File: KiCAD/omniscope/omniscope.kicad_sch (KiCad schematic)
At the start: 8 parts, among them J1 Conn_01x08_Male, J2 Conn_01x02_Male, J3 Conn_01x02_Male, J4 Conn_01x08_Male, J5 Conn_01x08_Male, J6 Conn_01x08_Male, J7 Conn_01x08_Male, J8 Conn_01x08_Male

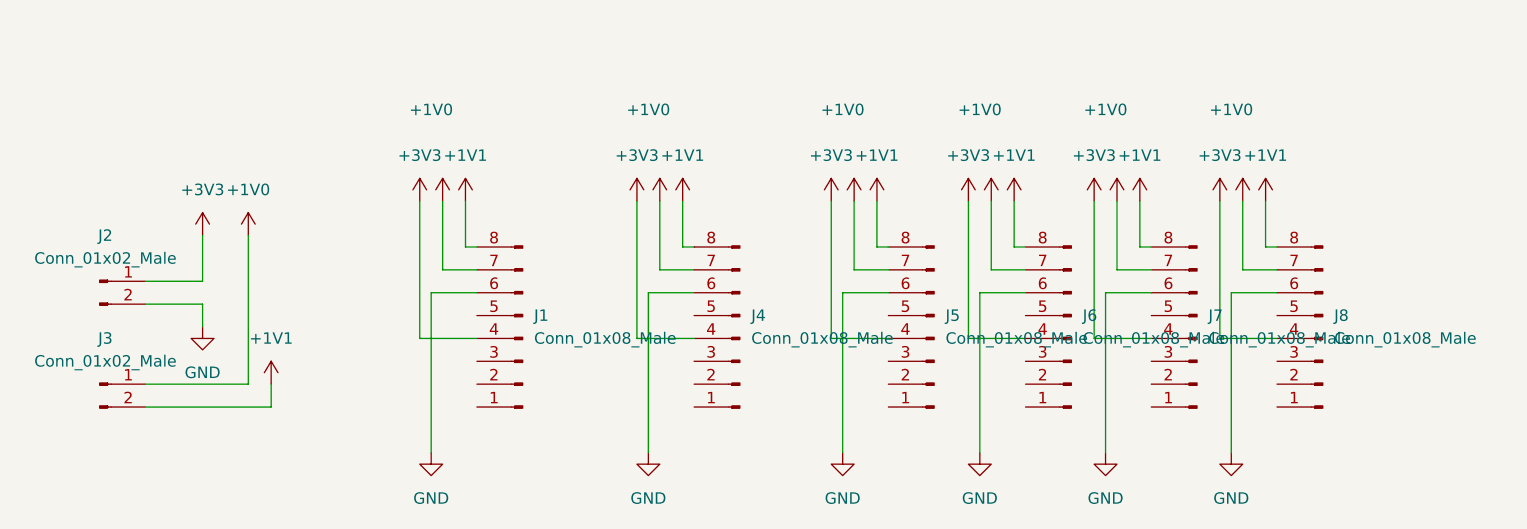
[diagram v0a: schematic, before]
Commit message: Adding PCB for SD Card
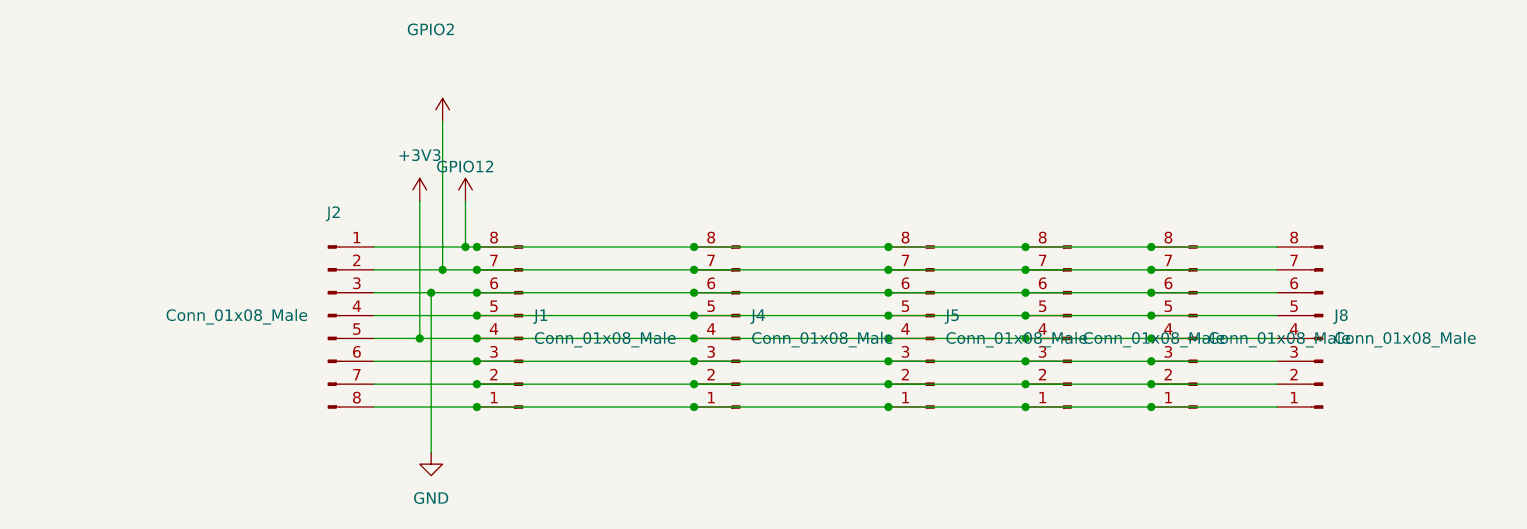
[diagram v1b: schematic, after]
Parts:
- removed J2, J3: Conn_01x02_Male, Connector_PinHeader_2.54mm:PinHeader_1x02_P2.54mm_Vertical, symbol Connector:Conn_01x02_Male
- added J2: Conn_01x08_Male, Connector_PinHeader_2.54mm:PinHeader_1x08_P2.54mm_Vertical, symbol Connector:Conn_01x08_Male
- J1, J4, J5, J6, J7, J8: footprint footprints:microSD_pinspacing -> Connector_PinHeader_2.54mm:PinHeader_1x08_P2.54mm_Vertical
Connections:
- net +1V0: now also J2.2 (Pin_2)
- net +1V1: now also J2.1 (Pin_1)
- net +3V3: now also J2.5 (Pin_5)
- net GND: now also J2.3 (Pin_3)
- net at J1.1 (Pin_1): now also J4.1 (Pin_1), J5.1 (Pin_1), J6.1 (Pin_1), J7.1 (Pin_1), J8.1 (Pin_1), J2.8 (Pin_8)
- net at J1.2 (Pin_2): now also J4.2 (Pin_2), J5.2 (Pin_2), J6.2 (Pin_2), J7.2 (Pin_2), J8.2 (Pin_2), J2.7 (Pin_7)
- net at J1.3 (Pin_3): now also J4.3 (Pin_3), J5.3 (Pin_3), J6.3 (Pin_3), J7.3 (Pin_3), J8.3 (Pin_3), J2.6 (Pin_6)
- net at J1.5 (Pin_5): now also J4.5 (Pin_5), J5.5 (Pin_5), J6.5 (Pin_5), J7.5 (Pin_5), J8.5 (Pin_5), J2.4 (Pin_4)

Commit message: Adding latest CAD Drawings
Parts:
- J1, J4, J5, J6, J7, J8: footprint Connector_PinHeader_2.54mm:PinHeader_1x08_P2.54mm_Vertical -> Connector_USB:USB_3.1_Brick_nogging_24_Male_Type-C_SMD_C399939
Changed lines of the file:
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@@
       (effects (font (size 1.27 1.27)) (justify right))
     )
-    (property "Footprint" "Connector_PinHeader_2.54mm:PinHeader_1x08_P2.54mm_Vertical" (at 81.28 57.15 0)
-      (effects (font (size 1.27 1.27)) hide)
-    )
-    (property "Datasheet" "~" (at 81.28 57.15 0)
+    (property "Footprint" "Connector_USB:USB_3.1_Brick_nogging_24_Male_Type-C_SMD_C399939" (at 81.28 57.15 0)
+      (effects (font (size 1.27 1.27)) hide)
+    )
+    (property "Datasheet" "  (layer \"F.Cu\")" (at 81.28 57.15 0)
       (effects (font (size 1.27 1.27)) hide)
     )
@@
       (effects (font (size 1.27 1.27)) (justify right))
     )
-    (property "Footprint" "Connector_PinHeader_2.54mm:PinHeader_1x08_P2.54mm_Vertical" (at 142.24 57.15 0)
+    (property "Footprint" "Connector_USB:USB_3.1_Brick_nogging_24_Male_Type-C_SMD_C399939" (at 142.24 57.15 0)
       (effects (font (size 1.27 1.27)) hide)
     )
@@
       (effects (font (size 1.27 1.27)) (justify right))
     )
-    (property "Footprint" "Connector_PinHeader_2.54mm:PinHeader_1x08_P2.54mm_Vertical" (at 105.41 57.15 0)
+    (property "Footprint" "Connector_USB:USB_3.1_Brick_nogging_24_Male_Type-C_SMD_C399939" (at 105.41 57.15 0)
       (effects (font (size 1.27 1.27)) hide)
     )
@@
       (effects (font (size 1.27 1.27)) (justify right))
     )
-    (property "Footprint" "Connector_PinHeader_2.54mm:PinHeader_1x08_P2.54mm_Vertical" (at 170.18 57.15 0)
+    (property "Footprint" "Connector_USB:USB_3.1_Brick_nogging_24_Male_Type-C_SMD_C399939" (at 170.18 57.15 0)
       (effects (font (size 1.27 1.27)) hide)
     )
@@
       (effects (font (size 1.27 1.27)) (justify right))
     )
-    (property "Footprint" "Connector_PinHeader_2.54mm:PinHeader_1x08_P2.54mm_Vertical" (at 127 57.15 0)
+    (property "Footprint" "Connector_USB:USB_3.1_Brick_nogging_24_Male_Type-C_SMD_C399939" (at 127 57.15 0)
       (effects (font (size 1.27 1.27)) hide)
     )
@@
       (effects (font (size 1.27 1.27)) (justify right))
     )
-    (property "Footprint" "Connector_PinHeader_2.54mm:PinHeader_1x08_P2.54mm_Vertical" (at 156.21 57.15 0)
-      (effects (font (size 1.27 1.27)) hide)
-    )
+    (property "Footprint" "Connector_USB:USB_3.1_Brick_nogging_24_Male_Type-C_SMD_C399939" (at 156.21 57.15 0)
+      (effects (font (size 1.27 1.27)) hide)
+    )
